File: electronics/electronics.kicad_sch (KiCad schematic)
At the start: 9 parts, among them SW1 Button, U1 ESP32-WROOM-32, U2 MIKROE_click

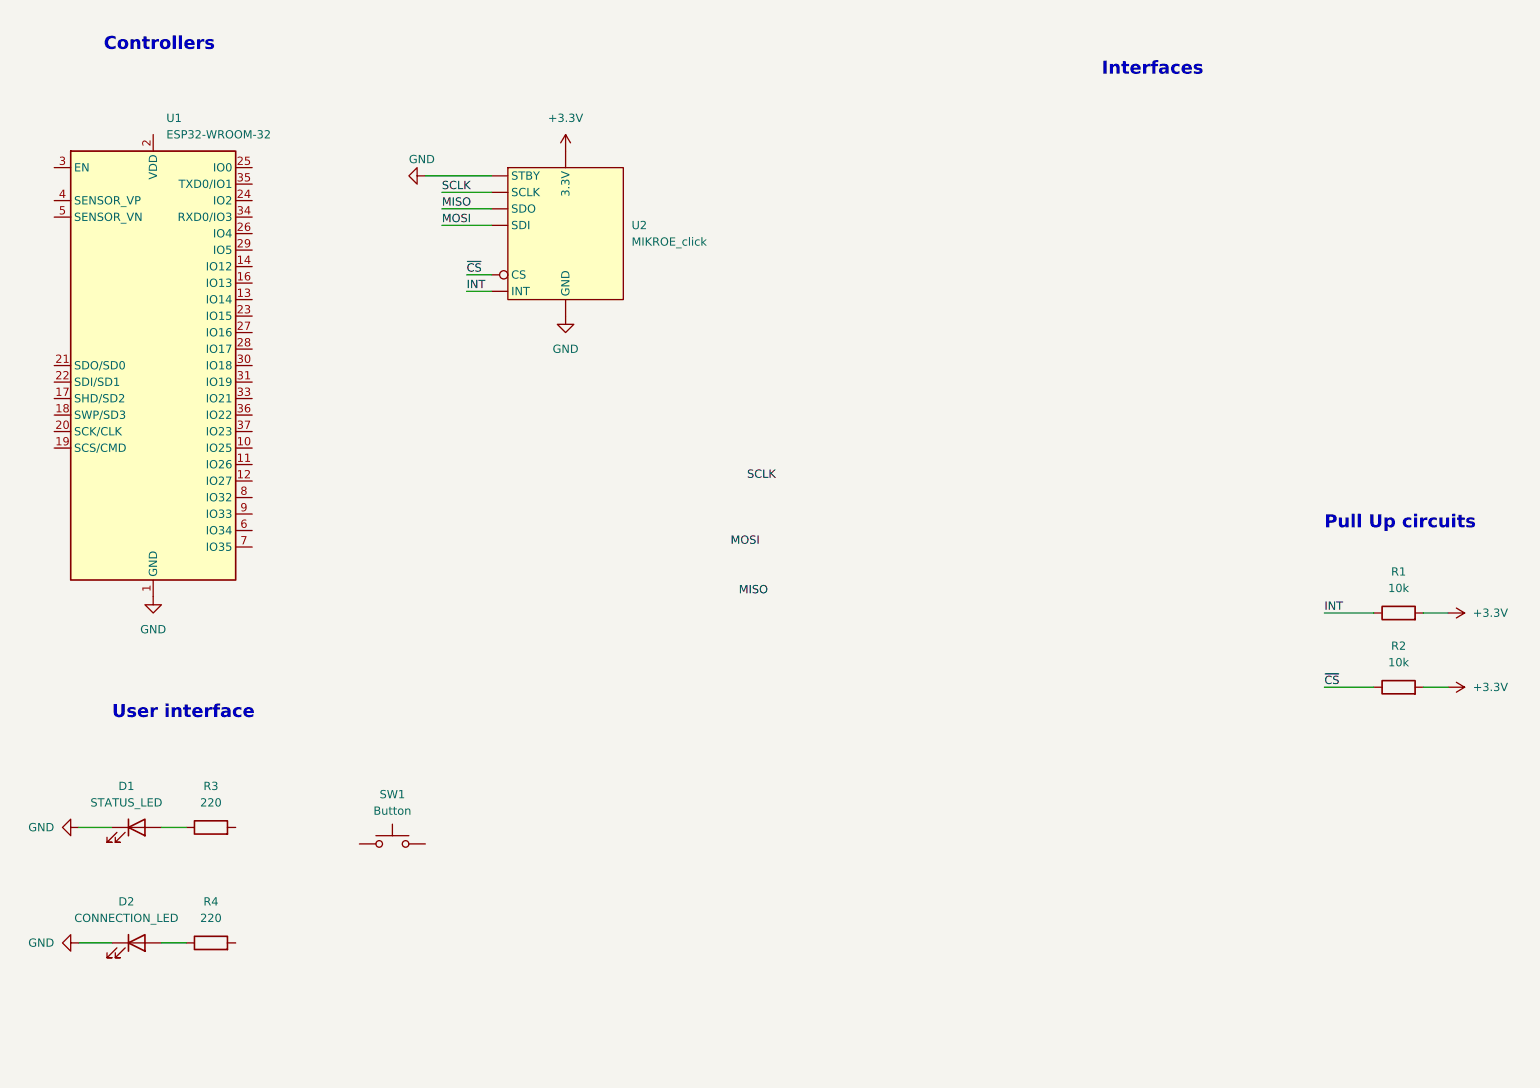
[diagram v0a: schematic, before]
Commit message: added complete circuit electronics
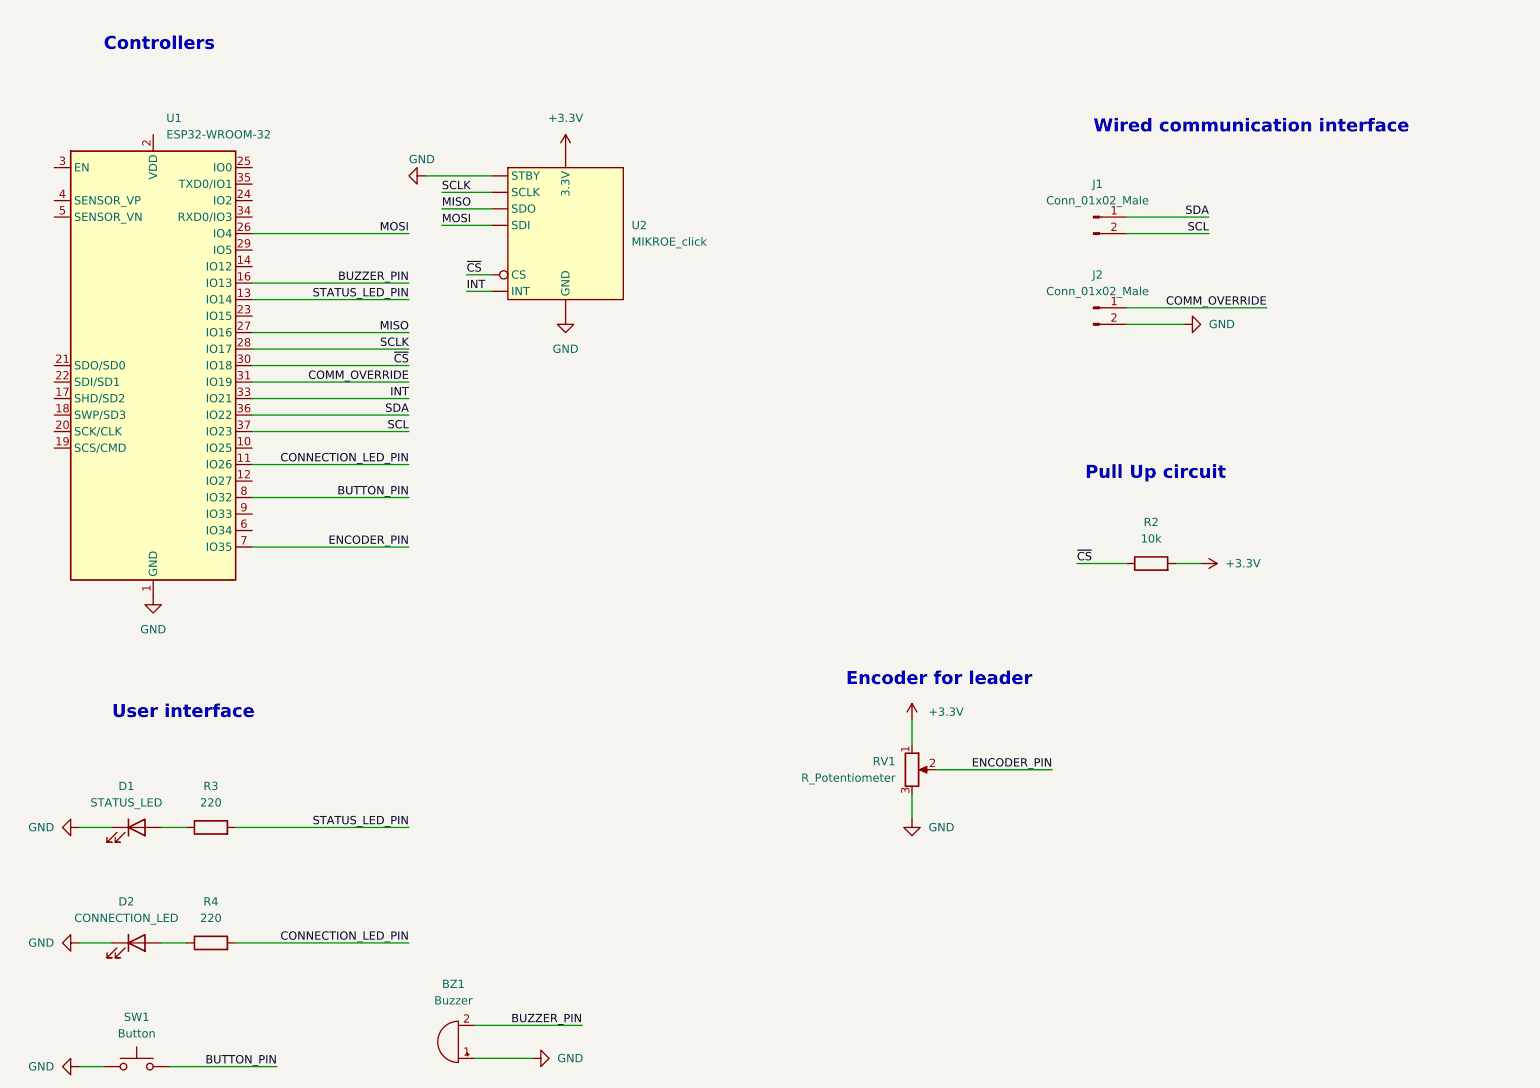
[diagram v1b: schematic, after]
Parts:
- removed R1: 10k, symbol Device:R
- added BZ1: Buzzer, symbol Device:Buzzer
- added J1, J2: Conn_01x02_Male, symbol Connector:Conn_01x02_Male
- added RV1: R_Potentiometer, symbol Device:R_Potentiometer
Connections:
- net +3.3V: now also RV1.1
- net GND: now also SW1.1, BZ1.1 (-), J2.2 (Pin_2), RV1.3
- net INT: now also U1.33 (IO21)
- net MISO: now also U1.27 (IO16)
- net MOSI: now also U1.26 (IO4)
- net SCLK: now also U1.28 (IO17)
- net ~{CS}: now also U1.30 (IO18)
- net BUTTON_PIN: now reaches SW1.2
- net BUTTON_PIN: now also U1.8 (IO32)
- net CONNECTION_LED_PIN: now reaches U1.11 (IO26)
- net CONNECTION_LED_PIN: now also R4.2
- net STATUS_LED_PIN: now reaches U1.13 (IO14)
- net STATUS_LED_PIN: now also R3.2
- net BUZZER_PIN: now reaches U1.16 (IO13)
- net BUZZER_PIN: now also BZ1.2 (+)
- net COMM_OVERRIDE: now reaches U1.31 (IO19)
- net COMM_OVERRIDE: now also J2.1 (Pin_1)
- net SDA: now reaches U1.36 (IO22)
- net SDA: now also J1.1 (Pin_1)
- net SCL: now reaches U1.37 (IO23)
- net SCL: now also J1.2 (Pin_2)
- net ENCODER_PIN: now reaches U1.7 (IO35)
- net ENCODER_PIN: now also RV1.2
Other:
- note added: "Encoder for leader"
- note added: "Pull Up circuit"
- note added: "Wired communication interface"
- note removed: "Interfaces"
- note removed: "Pull Up circuits"
- moved on the sheet: R2, SW1

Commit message: modified looks of electronics
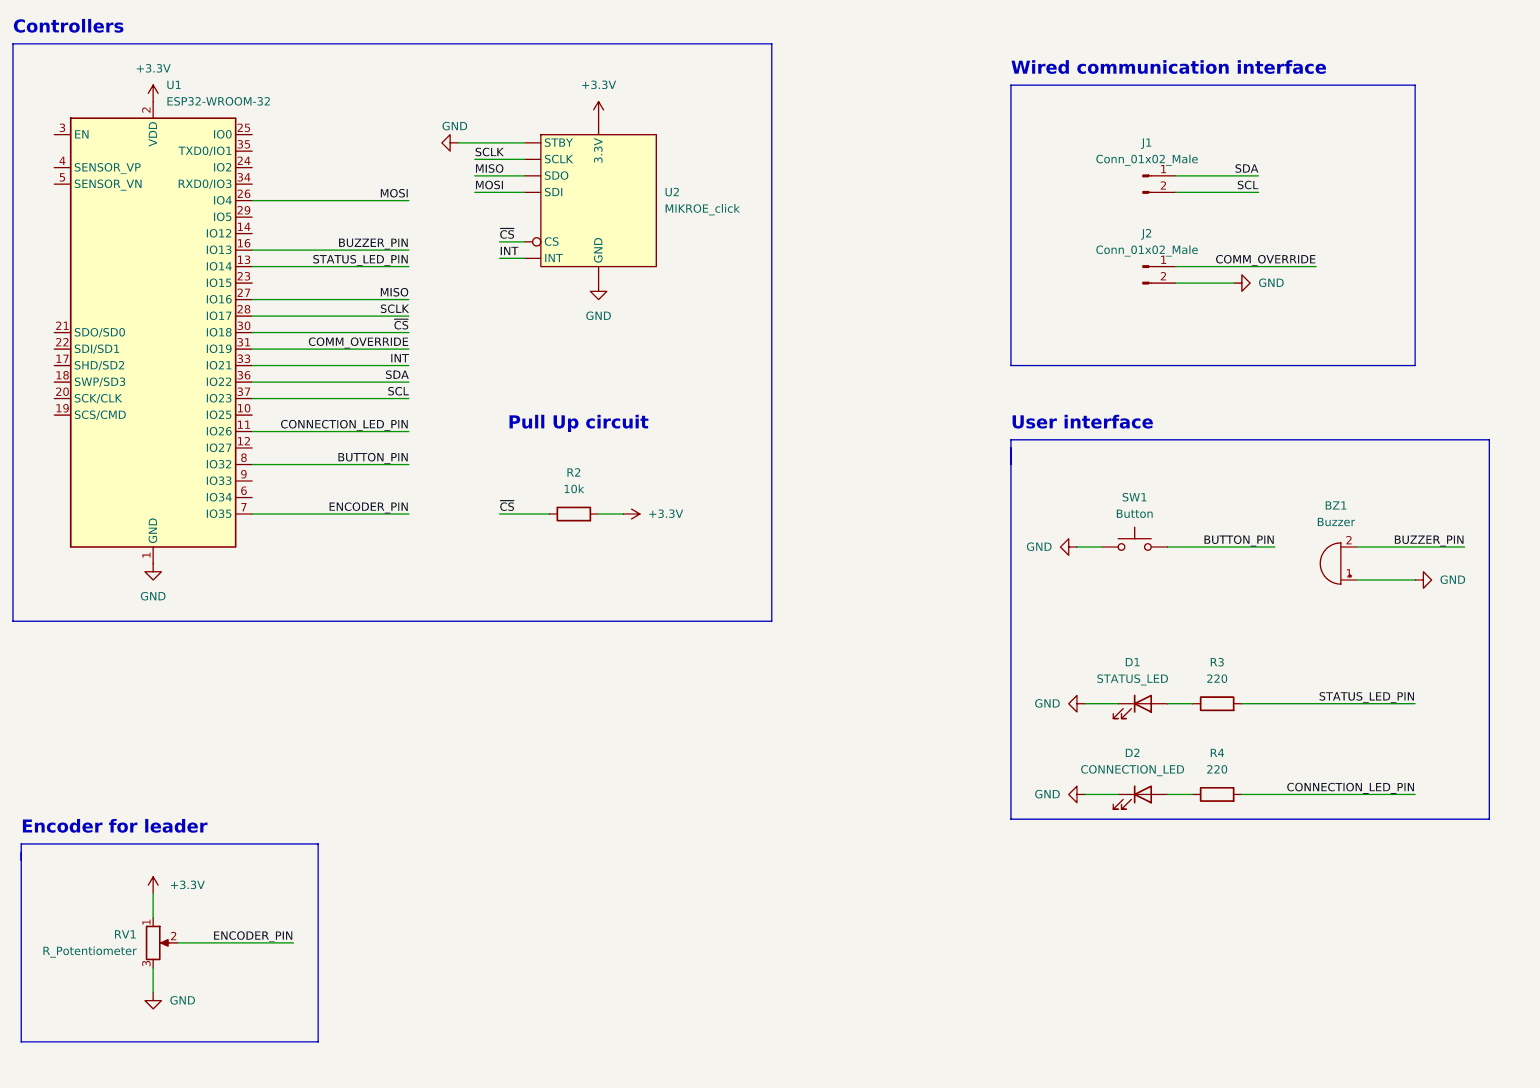
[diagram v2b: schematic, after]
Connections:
- net +3.3V: now also U1.2 (VDD)
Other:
- company: (none) -> Group 3 - ME410
- title: (none) -> Electronics of SyncRower
- moved on the sheet: BZ1, D1, D2, J1, J2, R2, R3, R4, RV1, SW1, U1, U2
